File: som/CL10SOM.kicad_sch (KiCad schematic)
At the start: 53 parts, among them IC1 10CL025YU256C8G, J1 Conn_01x02_Pin, U1 MT46H32M16LFBF-5 IT:C, U2 MX25L12833FM2, U6 AT93C46DN-SH-T, U7 SG3225CAN 50.0000M-TJGA6, X1 DF40C-120DS-0.4V51

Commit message: Work in progress
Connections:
- net X1_10 is gone; now on net VCCB4: X1.10
- net X1_12 is gone; now on net VCCB5: X1.12
- net X1_2 is gone; now on net GND: X1.2
- net X1_4 is gone; now on net GND: X1.4
- net X1_6 is gone; now on net VCCB2: X1.6
- net X1_8 is gone; now on net VCCB3: X1.8
- net +3.3V: no longer C7.1, IC1.A16 (VCCIO7_1), IC1.E14 (VCCIO6_1), IC1.G14 (VCCIO6_2)
- net +3V3: now also C7.1, IC1.A16 (VCCIO7_1), IC1.E14 (VCCIO6_1), IC1.G14 (VCCIO6_2)
- net DDR_A1: now also IC1.A12 (IO/DIFFIO_T21n); no longer IC1.A4 (IO/DIFFIO_T3n)
- net DDR_A11: now also IC1.B4 (IO/DIFFIO_T3p); no longer IC1.A12 (IO/DIFFIO_T21n)
- net DDR_A3: now also IC1.A13 (IO/DIFFIO_T22n); no longer IC1.A6 (IO/DIFFIO_T7n/DPCLK11)
- net DDR_A4: now also IC1.A2 (IO/DIFFIO_T2n); no longer IC1.A15 (IO/DIFFIO_T19n)
- net DDR_A6: now also IC1.A4 (IO/DIFFIO_T3n); no longer IC1.A13 (IO/DIFFIO_T22n)
- net DDR_A7: now also IC1.B3 (IO/CDPCLK7); no longer IC1.B14 (IO/PLL2_CLKOUTp)
- net DDR_A9: now also IC1.A5 (IO/DIFFIO_T5n/DATA7); no longer IC1.B13 (IO/DIFFIO_T22p)
- net DDR_BA1: now also IC1.A15 (IO/DIFFIO_T19n); no longer IC1.A2 (IO/DIFFIO_T2n)
- net DDR_CKE: now also IC1.A6 (IO/DIFFIO_T7n/DPCLK11); no longer IC1.B4 (IO/DIFFIO_T3p)
- net DDR_DQ5: now also IC1.B13 (IO/DIFFIO_T22p); no longer IC1.A5 (IO/DIFFIO_T5n/DATA7)
- net GND: now also X1.3
- net TCK: no longer X1.3
- net TDI: no longer X1.9
- net TDO: no longer X1.5
- net TMS: no longer X1.7
- net ~{DDR_RAS}: now also IC1.B14 (IO/PLL2_CLKOUTp); no longer IC1.B3 (IO/CDPCLK7)
- net X1_13: no longer names the net of X1.13
- net X1_14: no longer names the net of X1.14
- net X1_15: no longer names the net of X1.15
- net X1_16: no longer names the net of X1.16
- net X1_17: no longer names the net of X1.17
- net X1_18: no longer names the net of X1.18
- net X1_19: no longer names the net of X1.19
- net X1_20: no longer names the net of X1.20
- net X1_21: no longer names the net of X1.21
- net X1_22: no longer names the net of X1.22
- net X1_23: no longer names the net of X1.23
- net X1_24: no longer names the net of X1.24
- net X1_25: no longer names the net of X1.25
- net X1_26: no longer names the net of X1.26
- net X1_27: no longer names the net of X1.27
- net X1_28: no longer names the net of X1.28
- net X1_29: no longer names the net of X1.29
- net X1_30: no longer names the net of X1.30
- net X1_31: no longer names the net of X1.31
- net X1_32: no longer names the net of X1.32
- net X1_33: no longer names the net of X1.33
- net X1_34: no longer names the net of X1.34
- net X1_35: no longer names the net of X1.35
- net X1_36: no longer names the net of X1.36
- net X1_37: no longer names the net of X1.37
- net X1_38: no longer names the net of X1.38
- net X1_39: no longer names the net of X1.39
- net X1_40: no longer names the net of X1.40

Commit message: Work in progress
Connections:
- net DDR_A0: now also IC1.E8 (IO/DIFFIO_T10n/DATA2); no longer IC1.D12 (IO/DIFFIO_T23p/CDPCLK6)
- net DDR_A1: now also IC1.A5 (IO/DIFFIO_T5n/DATA7); no longer IC1.A12 (IO/DIFFIO_T21n)
- net DDR_A10: now also IC1.B5 (IO/DIFFIO_T5p); no longer IC1.A14 (IO/PLL2_CLKOUTn)
- net DDR_A12: now also IC1.A7 (IO/DIFFIO_T9n); no longer IC1.A3 (IO/DIFFIO_T2p)
- net DDR_A13: now also IC1.F8 (IO/DIFFIO_T10p/DATA3); no longer IC1.C8 (IO/DIFFIO_T11p/DPCLK10)
- net DDR_A2: now also IC1.D6 (IO/DIFFIO_T4n); no longer IC1.B12 (IO/DIFFIO_T21p)
- net DDR_A3: now also IC1.E6 (IO/DIFFIO_T6p/DATA6); no longer IC1.A13 (IO/DIFFIO_T22n)
- net DDR_A5: now also IC1.A3 (IO/DIFFIO_T2p); no longer IC1.B7 (IO/DIFFIO_T9p/DATA4)
- net DDR_A8: now also IC1.B6 (IO/DIFFIO_T7p); no longer IC1.A11 (IO/DIFFIO_T20n)
- net DDR_A9: now also IC1.B7 (IO/DIFFIO_T9p/DATA4); no longer IC1.A5 (IO/DIFFIO_T5n/DATA7)
- net DDR_BA0: now also IC1.C6 (IO/VREFB8N0); no longer IC1.D11 (IO/DIFFIO_T23n)
- net DDR_BA1: now also IC1.F9 (IO/DIFFIO_T17p/DPCLK8); no longer IC1.A15 (IO/DIFFIO_T19n)
- net DDR_CKE: now also IC1.C8 (IO/DIFFIO_T11p/DPCLK10); no longer IC1.A6 (IO/DIFFIO_T7n/DPCLK11)
- net DDR_DM0: now also IC1.D9 (IO/DIFFIO_T15p); no longer IC1.D14 (IO/DIFFIO_T24p)
- net DDR_DM1: now also IC1.D12 (IO/DIFFIO_T23p/CDPCLK6); no longer IC1.C14 (IO/DIFFIO_T24n)
- net DDR_DQ0: now also IC1.C14 (IO/DIFFIO_T24n); no longer IC1.F8 (IO/DIFFIO_T10p/DATA3)
- net DDR_DQ1: now also IC1.B12 (IO/DIFFIO_T21p); no longer IC1.C6 (IO/VREFB8N0)
- net DDR_DQ10: now also IC1.C11 (IO/VREFB7N0); no longer IC1.F9 (IO/DIFFIO_T17p/DPCLK8)
- net DDR_DQ11: now also IC1.B14 (IO/PLL2_CLKOUTp); no longer IC1.B10 (IO/DIFFIO_T16p)
- net DDR_DQ12: now also IC1.A15 (IO/DIFFIO_T19n); no longer IC1.C9 (IO/DIFFIO_T15n)
- net DDR_DQ13: now also IC1.A14 (IO/PLL2_CLKOUTn); no longer IC1.E9 (IO/DIFFIO_T13p/DPCLK9)
- net DDR_DQ14: now also IC1.A13 (IO/DIFFIO_T22n); no longer IC1.E10 (IO/RDN4)
- net DDR_DQ15: now also IC1.B13 (IO/DIFFIO_T22p); no longer IC1.B11 (IO/DIFFIO_T20p)
- net DDR_DQ2: now also IC1.D14 (IO/DIFFIO_T24p); no longer IC1.B6 (IO/DIFFIO_T7p)
- net DDR_DQ3: now also IC1.B11 (IO/DIFFIO_T20p); no longer IC1.B5 (IO/DIFFIO_T5p)
- net DDR_DQ4: now also IC1.A12 (IO/DIFFIO_T21n); no longer IC1.D6 (IO/DIFFIO_T4n)
- net DDR_DQ5: now also IC1.A11 (IO/DIFFIO_T20n); no longer IC1.B13 (IO/DIFFIO_T22p)
- net DDR_DQ6: now also IC1.E11 (IO/RUP4); no longer IC1.D8 (IO)
- net DDR_DQ7: now also IC1.E10 (IO/RDN4); no longer IC1.A7 (IO/DIFFIO_T9n)
- net DDR_DQ8: now also IC1.B10 (IO/DIFFIO_T16p); no longer IC1.D9 (IO/DIFFIO_T15p)
- net DDR_DQ9: now also IC1.A10 (IO/DIFFIO_T16n); no longer IC1.C11 (IO/VREFB7N0)
- net DDR_DQS0: now also IC1.D11 (IO/DIFFIO_T23n); no longer IC1.E7 (IO/DATA5)
- net DDR_DQS1: now also IC1.C9 (IO/DIFFIO_T15n); no longer IC1.E8 (IO/DIFFIO_T10n/DATA2)
- net ~{DDR_CAS}: now also IC1.A6 (IO/DIFFIO_T7n/DPCLK11); no longer IC1.A10 (IO/DIFFIO_T16n)
- net ~{DDR_CS}: now also IC1.E7 (IO/DATA5); no longer IC1.E11 (IO/RUP4)
- net ~{DDR_RAS}: now also IC1.D8 (IO); no longer IC1.B14 (IO/PLL2_CLKOUTp)
- net ~{DDR_WE}: now also IC1.E9 (IO/DIFFIO_T13p/DPCLK9); no longer IC1.E6 (IO/DIFFIO_T6p/DATA6)

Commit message: Work in progress
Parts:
- removed unit 3 of X1
- removed unit 2 of X1
- added C18: 100nF, Capacitor_SMD:C_0603_1608Metric, symbol Sheet1-altium-import:root_1_C_0805
- added TP1, TP2, TP3, TP4: TestPoint_Small, TestPoint:TestPoint_Pad_D1.0mm, symbol Connector:TestPoint_Small
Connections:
- net B1-CLK0 is gone; now on net CLC50: IC1.E2 (CLK0/DIFFCLK_0p)
- net B1-IO1 is gone; now on net EECS: IC1.B1 (IO/CDPCLK0)
- net B1-IO2 is gone; now on net EECK: IC1.C2 (IO/DIFFIO_L3p)
- net B1-IO3 is gone; now on net EEDO: IC1.F3 (IO/VREFB1N0)
- net B1-IO4 is gone; now on net EEDI: IC1.D1 (IO/DIFFIO_L4n)
- net +1V8: now also X1.17, X1.19
- net +2V5: now also X1.13, X1.15
- net +3.3V: now also X1.9; no longer R49.2, R60.2
- net +3V3: now also R49.2, R60.2, C18.1
- net +5V: now also X1.1, X1.3, X1.5, X1.7
- net B6-CLK4: now also X1.98
- net B6-CLK5: now also X1.100
- net B6-IO1: now also X1.101
- net B6-IO10: now also X1.108
- net B6-IO11: now also X1.110
- net B6-IO2: now also X1.103
- net B6-IO3: now also X1.105
- net B6-IO4: now also X1.107
- net B6-IO5: now also X1.109
- net B6-IO6: now also X1.111
- net B6-IO7: now also X1.102
- net B6-IO8: now also X1.104
- net B6-IO9: now also X1.106
- net B7-CLK8: now also TP1.1
- net B7-CLK9: now also TP2.1
- net B8-CLK10: now also TP3.1
- net B8-CLK11: now also TP4.1
- net GND: now also X1.6, X1.8, C18.2; no longer X1.1, X1.3
- net TCK: now also X1.116
- net TDI: now also X1.114
- net TDO: now also X1.115
- net TMS: now also X1.113
- net VCCB2: now also X1.10; no longer X1.6
- net VCCB3: now also X1.12; no longer X1.8
- net VCCB4: now also X1.14; no longer X1.10
- net VCCB5: now also X1.16; no longer X1.12

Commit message: Placement change
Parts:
- removed TP1, TP2, TP3, TP4: TestPoint_Small, TestPoint:TestPoint_Pad_D1.0mm, symbol Connector:TestPoint_Small
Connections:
- net B2-IO10 is gone; now on net B2-IO6: IC1.K5 (IO/RUP1)
- net B2-IO11 is gone; now on net B2-IO7: IC1.L4 (IO/RDN1)
- net B2-IO12 is gone; now on net B2-IO8: IC1.R1 (IO/CDPCLK1)
- net B3-IO10 is gone; now on net B3-IO7: IC1.M6 (IO)
- net B3-IO11 is gone; now on net B3-IO8: IC1.P6 (IO/VREFB3N0)
- net B3-IO17 is gone; now on net B3-IO12: IC1.L7 (IO)
- net B3-IO20 is gone; now on net B3-IO14: IC1.L8 (IO/DIFFIO_B9n)
- net B3-IO21 is gone; now on net B3-IO15: IC1.M8 (IO/DIFFIO_B10n)
- net B3-IO22 is gone; now on net B3-IO15: IC1.N8 (IO/DIFFIO_B11p)
- net B3-IO23 is gone; now on net B3-IO16: IC1.P8 (IO/DIFFIO_B12n)
- net B3-IO5 is gone; now on net B3-IO3: IC1.T2 (IO/CDPCLK2)
- net B4-IO12 is gone; now on net B4-IO8: IC1.M10 (IO/RUP2)
- net B4-IO13 is gone; now on net B4-IO9: IC1.N11 (IO/RDN2)
- net B4-IO16 is gone; now on net B4-IO11: IC1.N12 (IO/DIFFIO_B24p)
- net B5-IO12 is gone; now on net B5-IO8p: IC1.K15 (IO/DIFFIO_R10p)
- net B5-IO15 is gone; now on net B5-IO10: IC1.J14 (IO/DIFFIO_R8n)
- net B5-IO16 is gone; now on net B5-IO11: IC1.J13 (IO/DIFFIO_R7n)
- net B5-IO3 is gone; now on net B5-IO3n: IC1.P16 (IO/DIFFIO_R15n/CDPCLK4)
- net B5-IO4 is gone; now on net B5-IO3p: IC1.R16 (IO/DIFFIO_R15p)
- net B5-IO7 is gone; now on net B5-IO5: IC1.L14 (IO/VREFB5N0)
- net B5-IO8 is gone; now on net B5-IO6: IC1.L13 (IO/DIFFIO_R12p)
- net B5-IO9 is gone; now on net B5-IO7n: IC1.L16 (IO/DIFFIO_R11n)
- net +1V8: now also X1.117, X1.119; no longer X1.17, X1.19
- net +2V5: now also X1.113, X1.115; no longer X1.13, X1.15
- net +3.3V: now also X1.109, X1.111; no longer X1.11, X1.9
- net B2-IO4: now also IC1.L3 (IO/VREFB2N0); no longer IC1.K1 (IO/DIFFIO_L10n)
- net B2-IO6: no longer IC1.L1 (IO/DIFFIO_L11n)
- net B2-IO7: no longer IC1.L3 (IO/VREFB2N0)
- net B2-IO8: no longer IC1.N2 (IO/DIFFIO_L13p)
- net B3-IO12: no longer IC1.M7 (IO/DIFFIO_B5p/DPCLK2)
- net B3-IO14: no longer IC1.T5 (IO/DIFFIO_B6n)
- net B3-IO15: no longer IC1.R6 (IO/DIFFIO_B7p)
- net B3-IO16: no longer IC1.T6 (IO/DIFFIO_B7n)
- net B3-IO3: no longer IC1.R3 (IO/DIFFIO_B2p)
- net B3-IO7: no longer IC1.T4 (IO/PLL1_CLKOUTn)
- net B3-IO8: no longer IC1.N5 (IO/DIFFIO_B4p)
- net B3-IO9: now also IC1.M7 (IO/DIFFIO_B5p/DPCLK2); no longer IC1.N6 (IO/DIFFIO_B4n)
- net B4-IO11: no longer IC1.T13 (IO/DIFFIO_B20n)
- net B4-IO5: now also IC1.P9 (IO/DPCLK5); no longer IC1.T11 (IO/DIFFIO_B17n)
- net B4-IO6: now also IC1.P11 (IO/VREFB4N0); no longer IC1.R12 (IO/DIFFIO_B18p)
- net B4-IO8: no longer IC1.P9 (IO/DPCLK5)
- net B4-IO9: no longer IC1.P11 (IO/VREFB4N0)
- net B5-CLK6: now also X1.89
- net B5-CLK7: now also X1.87
- net B5-IO1: now also X1.80
- net B5-IO10: now also X1.105; no longer IC1.L15 (IO/DIFFIO_R11p)
- net B5-IO11: now also X1.107; no longer IC1.K16 (IO/DIFFIO_R10n)
- net B5-IO2: now also X1.81
- net B5-IO5: now also X1.86; no longer IC1.N16 (IO/DIFFIO_R13n)
- net B5-IO6: now also X1.91; no longer IC1.N15 (IO/DIFFIO_R13p)
- net B6-CLK4: now also X1.100; no longer X1.98
- net B6-CLK5: now also X1.98; no longer X1.100
- net B6-IO2: now also IC1.F13 (IO), X1.92; no longer IC1.G15 (IO/DIFFIO_R5p/CRC_ERROR), X1.103
- net B6-IO4: now also IC1.B16 (IO/DPCLK7), X1.102; no longer IC1.F16 (IO/DIFFIO_R4n/nCEO), X1.107
- net B6-IO5: now also IC1.F14 (IO/VREFB6N0), X1.104; no longer IC1.F15 (IO/DIFFIO_R4p/CLKUSR), X1.109
- net B6-IO6: now also IC1.D16 (IO), X1.106; no longer IC1.B16 (IO/DPCLK7), X1.111
- net B6-IO7: now also IC1.D15 (IO), X1.108; no longer IC1.F14 (IO/VREFB6N0), X1.102
- net DDR_DQ12: now also IC1.A14 (IO/PLL2_CLKOUTn); no longer IC1.A15 (IO/DIFFIO_T19n)
- net DDR_DQ13: now also IC1.A15 (IO/DIFFIO_T19n); no longer IC1.A14 (IO/PLL2_CLKOUTn)
- net DDR_DQ3: now also IC1.A12 (IO/DIFFIO_T21n); no longer IC1.B11 (IO/DIFFIO_T20p)
- net DDR_DQ4: now also IC1.B11 (IO/DIFFIO_T20p); no longer IC1.A12 (IO/DIFFIO_T21n)
- net TCK: now also X1.10; no longer X1.116
- net TDI: now also X1.12; no longer X1.114
- net TDO: now also X1.9; no longer X1.115
- net TMS: now also X1.11; no longer X1.113
- net VCCB2: now also X1.114; no longer X1.10
- net VCCB3: now also X1.116; no longer X1.12
- net VCCB4: now also X1.118; no longer X1.14
- net VCCB5: now also X1.120; no longer X1.16
- net B6-IO8p: now reaches X1.112
- net B6-IO8p: now also IC1.C15 (IO/DIFFIO_R1p)
- net B5-IO4n: now reaches X1.82
- net B5-IO4n: now also IC1.N16 (IO/DIFFIO_R13n)
- net B5-IO3p: now reaches X1.83
- net B5-IO4p: now reaches X1.84
- net B5-IO4p: now also IC1.N15 (IO/DIFFIO_R13p)
- net B5-IO3n: now reaches X1.85
- net B6-IO1p: now reaches X1.88
- net B6-IO1p: now also IC1.G15 (IO/DIFFIO_R5p/CRC_ERROR)
- net B6-IO1n: now reaches X1.90
- net B6-IO1n: now also IC1.G16 (IO/DIFFIO_R5n/INIT_DONE)
- net B5-IO7p: now reaches X1.93
- net B5-IO7p: now also IC1.L15 (IO/DIFFIO_R11p)
- net B6-IO3n: now reaches X1.94
- net B6-IO3n: now also IC1.F16 (IO/DIFFIO_R4n/nCEO)
- net B5-IO7n: now reaches X1.95
- net B6-IO3p: now reaches X1.96
- net B6-IO3p: now also IC1.F15 (IO/DIFFIO_R4p/CLKUSR)
- net B5-IO8p: now reaches X1.97
- net B5-IO8n: now reaches X1.99
- net B5-IO8n: now also IC1.K16 (IO/DIFFIO_R10n)
- net B2-IO1 renamed B2-IO1p
- net B2-IO13 renamed B2-IO9p
- net B2-IO14 renamed B2-IO9n
- net B2-IO2 renamed B2-IO1n
- net B2-IO3 renamed B2-IO2p
- net B2-IO5 renamed B2-IO3p
- net B2-IO9 renamed B2-IO5n
- net B3-IO1 renamed B3-IO1p
- net B3-IO13 renamed B3-IO10p
- net B3-IO18 renamed B3-IO13p
- net B3-IO19 renamed B3-IO13n
- net B3-IO2 renamed B3-IO1n
- net B3-IO4 renamed B3-IO2n
- net B3-IO6 renamed B3-IO4-COp
- net B4-IO10 renamed B4-IO7p
- net B4-IO14 renamed B4-IO10p
- net B4-IO15 renamed B4-IO10n
- net B4-IO17 renamed B4-IO12-COp
- net B4-IO18 renamed B4-IO12-COn
- net B4-IO2 renamed B4-IO2p
- net B4-IO3 renamed B4-IO2n
- net B4-IO4 renamed B4-IO3p
- net B4-IO7 renamed B4-IO4n
- net B5-IO13 renamed B5-IO9n
- net B5-IO9n: now also X1.103
- net B5-IO14 renamed B5-IO9p
- net B5-IO9p: now also X1.101
- removed net B6-IO1: IC1.G16 (IO/DIFFIO_R5n/INIT_DONE), X1.101
- net B6-IO10 renamed B6-IO8n
- net B6-IO8n: now also X1.110; no longer X1.108
- removed net B6-IO11: IC1.C15 (IO/DIFFIO_R1p), X1.110
- removed net B6-IO3: IC1.F13 (IO), X1.105
- removed net B6-IO8: IC1.D16 (IO), X1.104
- removed net B6-IO9: IC1.D15 (IO), X1.106
- new net B2-IO2n: IC1.K1 (IO/DIFFIO_L10n)
- new net B2-IO3n: IC1.L1 (IO/DIFFIO_L11n)
- new net B2-IO5p: IC1.N2 (IO/DIFFIO_L13p)
- new net B3-IO10n: IC1.T5 (IO/DIFFIO_B6n)
- new net B3-IO11n: IC1.T6 (IO/DIFFIO_B7n)
- new net B3-IO11p: IC1.R6 (IO/DIFFIO_B7p)
- new net B3-IO2p: IC1.R3 (IO/DIFFIO_B2p)
- new net B3-IO5-COn: IC1.T4 (IO/PLL1_CLKOUTn)
- new net B3-IO6n: IC1.N6 (IO/DIFFIO_B4n)
- new net B3-IO6p: IC1.N5 (IO/DIFFIO_B4p)
- new net B4-IO3n: IC1.T11 (IO/DIFFIO_B17n)
- new net B4-IO4p: IC1.R12 (IO/DIFFIO_B18p)
- new net B4-IO7n: IC1.T13 (IO/DIFFIO_B20n)

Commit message: Work in progress
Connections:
- net B3-CLK14: now also X1.57
- net B3-CLK15: now also X1.55
- net B3-IO10n: now also X1.45
- net B3-IO10p: now also X1.43
- net B3-IO11n: now also X1.49
- net B3-IO11p: now also X1.47
- net B3-IO12: now also X1.48
- net B3-IO13n: now also X1.53
- net B3-IO13p: now also X1.51
- net B3-IO14: now also X1.62
- net B3-IO15: now also X1.54, X1.60
- net B3-IO16: now also X1.56
- net B3-IO1n: now also X1.40
- net B3-IO1p: now also X1.38
- net B3-IO2n: now also X1.37
- net B3-IO2p: now also X1.35
- net B3-IO3: now also X1.36
- net B3-IO4-COp: now also X1.39
- net B3-IO5-COn: now also X1.41
- net B3-IO6n: now also X1.44
- net B3-IO6p: now also X1.42
- net B3-IO7: now also X1.50
- net B3-IO8: now also X1.46
- net B3-IO9: now also X1.52
- net B4-CLK12: now also X1.61
- net B4-CLK13: now also X1.59
- net B4-IO1: now also X1.58
- net B4-IO10n: now also X1.79
- net B4-IO10p: now also X1.77
- net B4-IO11: now also X1.78
- net B4-IO12-COn: now also X1.75
- net B4-IO12-COp: now also X1.73
- net B4-IO2n: now also X1.68
- net B4-IO2p: now also X1.66
- net B4-IO3n: now also X1.67
- net B4-IO3p: now also X1.65
- net B4-IO4n: now also X1.71
- net B4-IO4p: now also X1.69
- net B4-IO5: now also X1.70
- net B4-IO6: now also X1.72
- net B4-IO7n: now also X1.76
- net B4-IO7p: now also X1.74
- net B4-IO8: now also X1.63
- net B4-IO9: now also X1.64

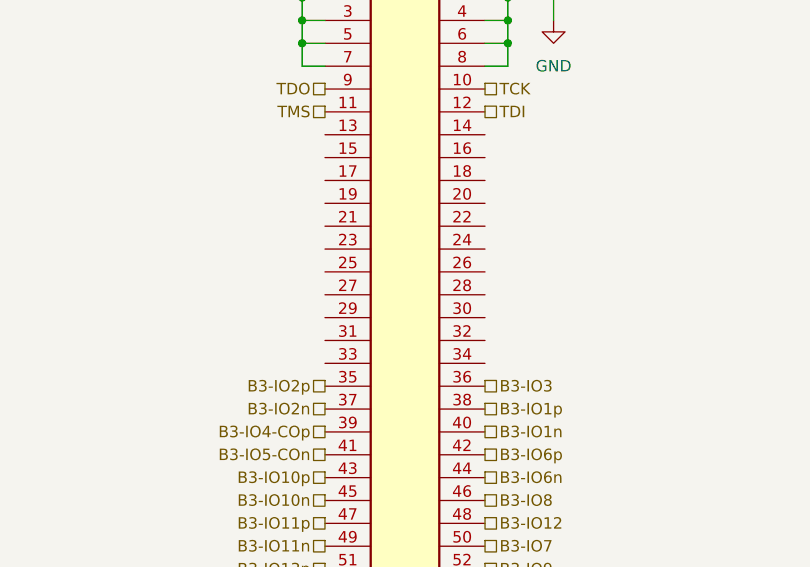
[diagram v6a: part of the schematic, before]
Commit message: All I/O connected
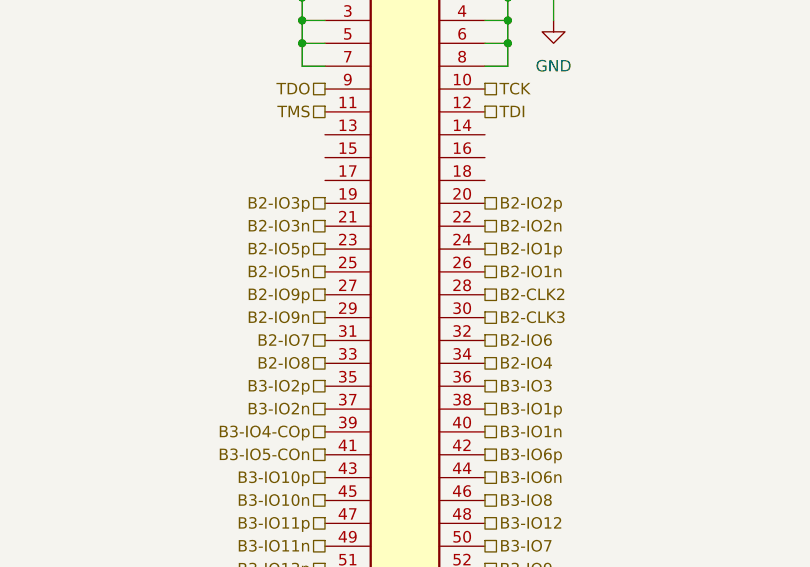
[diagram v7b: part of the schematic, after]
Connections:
- net B2-CLK2: now also X1.28
- net B2-CLK3: now also X1.30
- net B2-IO1n: now also X1.26
- net B2-IO1p: now also X1.24
- net B2-IO2n: now also X1.22
- net B2-IO2p: now also X1.20
- net B2-IO3n: now also X1.21
- net B2-IO3p: now also X1.19
- net B2-IO4: now also X1.34
- net B2-IO5n: now also X1.25
- net B2-IO5p: now also X1.23
- net B2-IO6: now also X1.32
- net B2-IO7: now also X1.31
- net B2-IO8: now also X1.33
- net B2-IO9n: now also X1.29
- net B2-IO9p: now also X1.27
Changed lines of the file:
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@@
+		)
+	)
+	(hierarchical_label "B2-IO1n"
+		(shape passive)
+		(at 422.91 237.49 0)
+		(effects
+			(font
+				(size 1.27 1.27)
+			)
+			(justify left)
 		)
 	)
@@
 		)
 	)
+	(hierarchical_label "B2-IO2p"
+		(shape passive)
+		(at 422.91 229.87 0)
+		(effects
+			(font
+				(size 1.27 1.27)
+			)
+			(justify left)
+		)
+	)
 	(hierarchical_label "B3-IO9"
 		(shape passive)
@@
 			)
 			(justify right)
+		)
+	)
+	(hierarchical_label "B2-IO1p"
+		(shape passive)
+		(at 422.91 234.95 0)
+		(effects
+			(font
+				(size 1.27 1.27)
+			)
+			(justify left)
 		)
 	)
@@
 		)
 	)
+	(hierarchical_label "B2-CLK2"
+		(shape passive)
+		(at 422.91 240.03 0)
+		(effects
+			(font
+				(size 1.27 1.27)
+			)
+			(justify left)
+		)
+	)
 	(hierarchical_label "~{DDR_CAS}"
 		(shape output)
@@
 		)
 	)
+	(hierarchical_label "B2-IO3p"
+		(shape passive)
+		(at 405.13 229.87 180)
+		(effects
+			(font
+				(size 1.27 1.27)
+			)
+			(justify right)
+		)
+	)
+	(hierarchical_label "B2-IO7"
+		(shape passive)
+		(at 405.13 245.11 180)
+		(effects
+			(font
+				(size 1.27 1.27)
+			)
+			(justify right)
+		)
+	)
 	(hierarchical_label "B4-CLK12"
 		(shape passive)
@@
 		)
 	)
+	(hierarchical_label "B2-IO8"
+		(shape passive)
+		(at 405.13 247.65 180)
+		(effects
+			(font
+				(size 1.27 1.27)
+			)
+			(justify right)
+		)
+	)
 	(hierarchical_label "B2-IO7"
 		(shape passive)
@@
 			)
 			(justify right)
+		)
+	)
+	(hierarchical_label "B2-IO2n"
+		(shape passive)
+		(at 422.91 232.41 0)
+		(effects
+			(font
+				(size 1.27 1.27)
+			)
+			(justify left)
 		)
 	)
@@
 		)
 	)
+	(hierarchical_label "B2-IO5p"
+		(shape passive)
+		(at 405.13 234.95 180)
+		(effects
+			(font
+				(size 1.27 1.27)
+			)
+			(justify right)
+		)
+	)
 	(hierarchical_label "B5-IO7p"
 		(shape passive)
@@
 		)
 	)
+	(hierarchical_label "B2-IO3n"
+		(shape passive)
+		(at 405.13 232.41 180)
+		(effects
+			(font
+				(size 1.27 1.27)
+			)
+			(justify right)
+		)
+	)
 	(hierarchical_label "B3-IO16"
 		(shape passive)
@@
 		)
 	)
+	(hierarchical_label "B2-IO4"
+		(shape passive)
+		(at 422.91 247.65 0)
+		(effects
+			(font
+				(size 1.27 1.27)
+			)
+			(justify left)
+		)
+	)
 	(hierarchical_label "B4-IO7n"
 		(shape passive)
@@
 		)
 	)
+	(hierarchical_label "B2-IO5n"
+		(shape passive)
+		(at 405.13 237.49 180)
+		(effects
+			(font
+				(size 1.27 1.27)
+			)
+			(justify right)
+		)
+	)
 	(hierarchical_label "B2-IO5p"
 		(shape passive)
@@
 		)
 	)
+	(hierarchical_label "B2-IO6"
+		(shape passive)
+		(at 422.91 245.11 0)
+		(effects
+			(font
+				(size 1.27 1.27)
+			)
+			(justify left)
+		)
+	)
 	(hierarchical_label "DDR_DQS0"
 		(shape input)
@@
 		)
 	)
+	(hierarchical_label "B2-CLK3"
+		(shape passive)
+		(at 422.91 242.57 0)
+		(effects
+			(font
+				(size 1.27 1.27)
+			)
+			(justify left)
+		)
+	)
 	(hierarchical_label "DDR_DQ6"
 		(shape bidirectional)
@@
 		)
 	)
+	(hierarchical_label "B2-IO9p"
+		(shape passive)
+		(at 405.13 240.03 180)
+		(effects
+			(font
+				(size 1.27 1.27)
+			)
+			(justify right)
+		)
+	)
 	(hierarchical_label "B3-IO3"
 		(shape passive)
@@
 		)
 	)
+	(hierarchical_label "B2-IO9n"
+		(shape passive)
+		(at 405.13 242.57 180)
+		(effects
+			(font
+				(size 1.27 1.27)
+			)
+			(justify right)
+		)
+	)

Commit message: Some cleanup
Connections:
- net B1-CLK1: now also X1.18
- net TDI: now also X1.9; no longer X1.12
- net TDO: now also X1.12; no longer X1.9
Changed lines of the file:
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@@
 	(hierarchical_label "TDO"
 		(shape passive)
-		(at 405.13 217.17 180)
-		(effects
-			(font
-				(size 1.27 1.27)
-			)
-			(justify right)
+		(at 422.91 219.71 0)
+		(effects
+			(font
+				(size 1.27 1.27)
+			)
+			(justify left)
 		)
 	)
@@
 		)
 	)
+	(hierarchical_label "B1-CLK1"
+		(shape passive)
+		(at 422.91 227.33 0)
+		(effects
+			(font
+				(size 1.27 1.27)
+			)
+			(justify left)
+		)
+	)
 	(hierarchical_label "DDR_DQ15"
 		(shape bidirectional)
@@
 	(hierarchical_label "TDI"
 		(shape passive)
-		(at 422.91 219.71 0)
-		(effects
-			(font
-				(size 1.27 1.27)
-			)
-			(justify left)
-		)
-	)
+		(at 405.13 217.17 180)
+		(effects
+			(font
+				(size 1.27 1.27)
+			)
+			(justify right)
+		)
+	)
